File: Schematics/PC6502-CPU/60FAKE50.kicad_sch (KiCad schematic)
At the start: 17 parts, among them J2 Conn_01x02, J3 USB_C_Receptacle_USB2.0_16P, Q1 IRLML6402, U9 FT245RNL

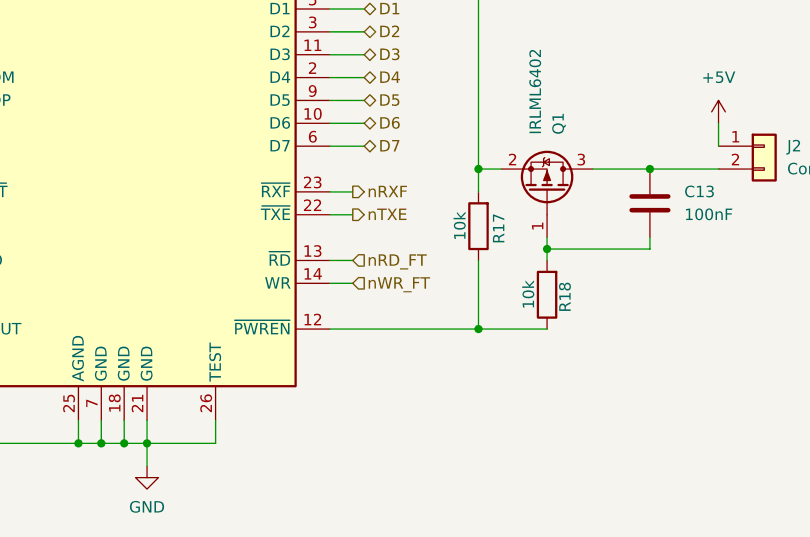
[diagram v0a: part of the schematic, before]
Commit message: FT245 label change
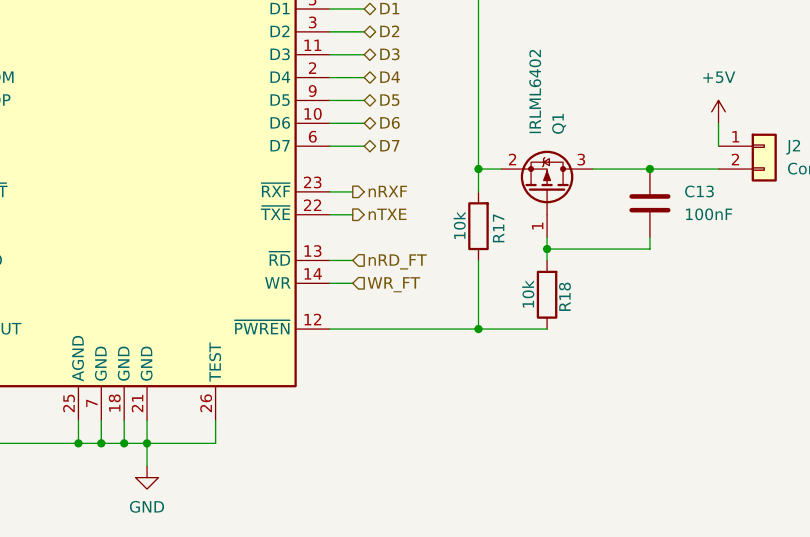
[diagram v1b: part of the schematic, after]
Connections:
- net nWR_FT renamed WR_FT
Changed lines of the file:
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@@
 		)
 	)
-	(hierarchical_label "nWR_FT"
+	(hierarchical_label "WR_FT"
 		(shape input)
 		(at 212.09 114.3 0)

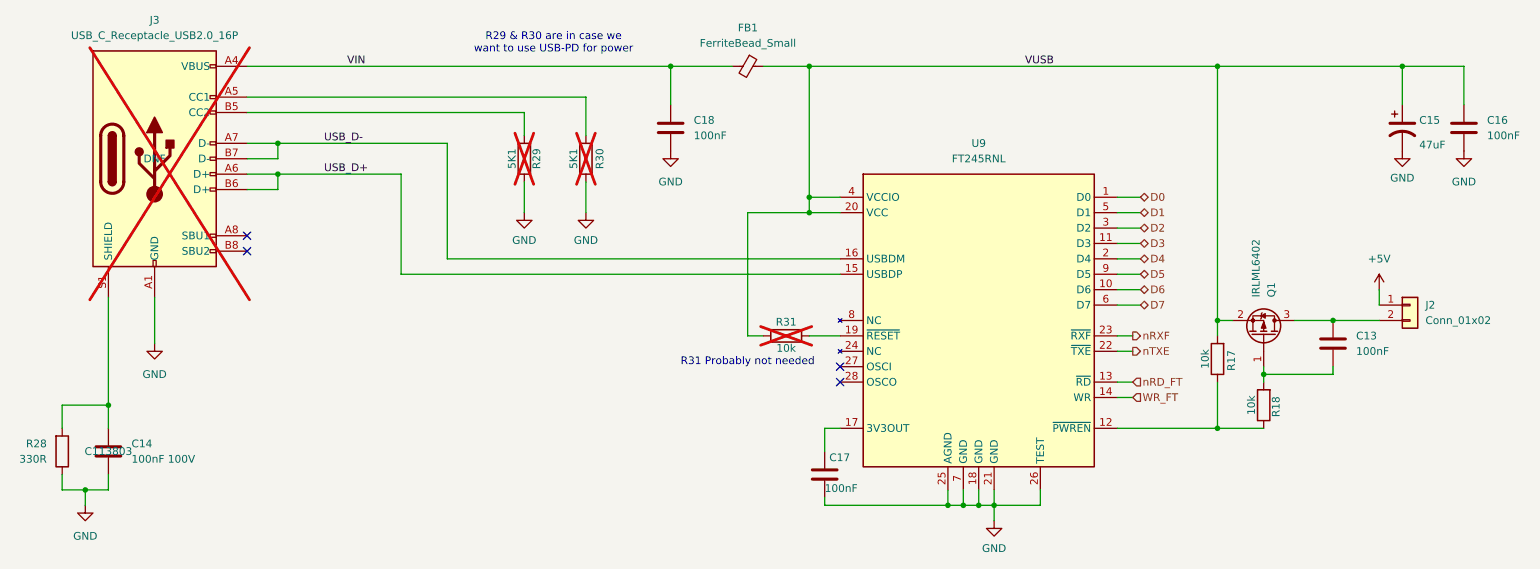
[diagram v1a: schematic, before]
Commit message: V1.1 CPU, VIA and POWER PCBs uploaded
A simpler CPU board (direct link to FT245R, 74161 removed and some tidying of tracks). Fixed a couple of floating inputs to RAM/ROM
VIA is much simpler, having just the one VIA chip.
POWER board has USB-PD and a 24VDC input for higher power stuff in the future.
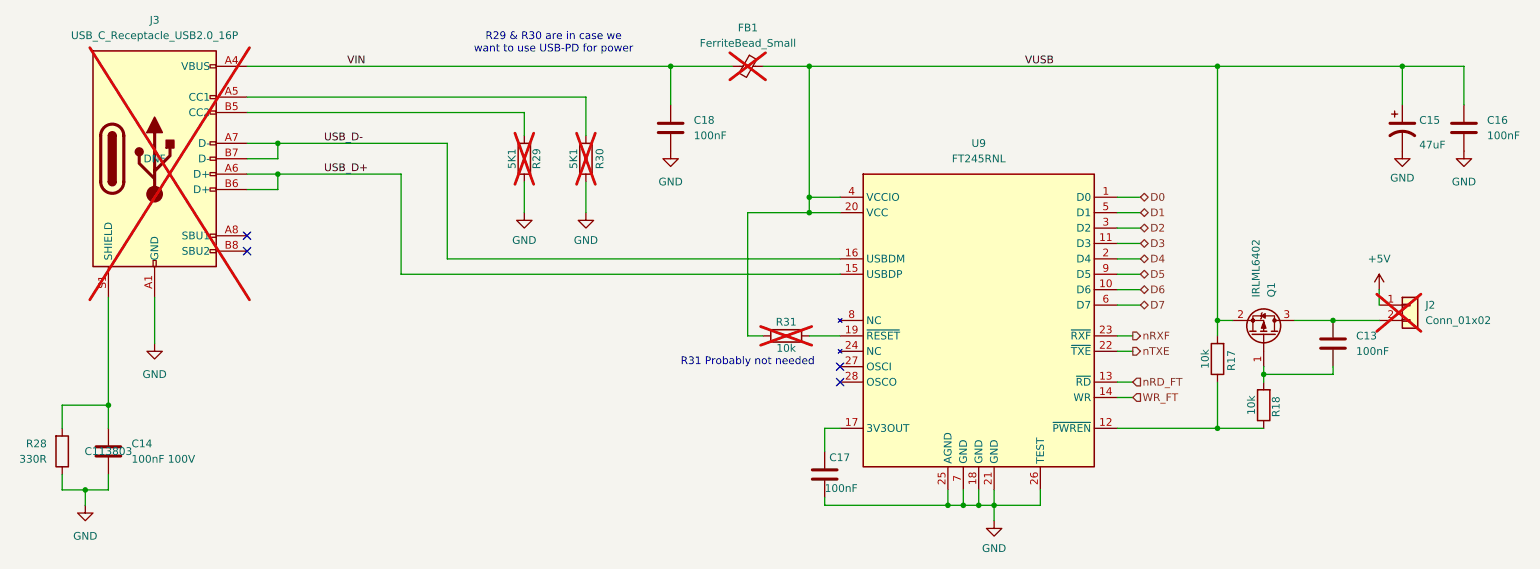
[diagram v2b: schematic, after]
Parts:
- C13, C17: LCSC (none) -> C113803
- C16, C18: LCSC (none) -> C49678
- FB1, J2: LCSC (none) -> DNF; now not fitted
- Q1: LCSC (none) -> C2593
- R17, R18: LCSC (none) -> C25744
- R28: LCSC (none) -> C25104
- R29, R30, R31: LCSC (none) -> DNF
- U9: LCSC (none) -> C6558294
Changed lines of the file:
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@@
 		(in_bom yes)
 		(on_board yes)
-		(dnp no)
+		(dnp yes)
 		(fields_autoplaced yes)
 		(property "Reference" "J2"
@@
 			)
 		)
+		(property "LCSC" "DNF"
+			(at 257.81 99.06 0)
+			(effects
+				(font
+					(size 1.27 1.27)
+				)
+				(hide yes)
+			)
+		)
 		(pin "1"
 		)
@@
 			)
 		)
+		(property "LCSC" "DNF"
+			(at 121.92 74.93 90)
+			(effects
+				(font
+					(size 1.27 1.27)
+				)
+				(hide yes)
+			)
+		)
 		(pin "1"
 		)
@@
 			)
 		)
+		(property "LCSC" "C25744"
+			(at 233.68 115.57 90)
+			(effects
+				(font
+					(size 1.27 1.27)
+				)
+				(hide yes)
+			)
+		)
 		(pin "1"
 		)
@@
 		)
 		(property "Description" ""
+			(at 161.29 127 0)
+			(effects
+				(font
+					(size 1.27 1.27)
+				)
+				(hide yes)
+			)
+		)
+		(property "LCSC" "C113803"
 			(at 161.29 127 0)
 			(effects
@@
 			)
 		)
+		(property "LCSC" "DNF"
+			(at 111.76 74.93 90)
+			(effects
+				(font
+					(size 1.27 1.27)
+				)
+				(hide yes)
+			)
+		)
 		(pin "1"
 		)
@@
 			)
 		)
-		(property "LCSC" ""
+		(property "LCSC" "C25104"
 			(at 35.56 123.19 0)
 			(effects
@@
 			)
 		)
+		(property "LCSC" "C6558294"
+			(at 186.69 101.6 0)
+			(effects
+				(font
+					(size 1.27 1.27)
+				)
+				(hide yes)
+			)
+		)
 		(pin "28"
 		)
@@
 			)
 		)
+		(property "LCSC" "DNF"
+			(at 154.94 104.14 90)
+			(effects
+				(font
+					(size 1.27 1.27)
+				)
+				(hide yes)
+			)
+		)
 		(pin "1"
 		)
@@
 		(property "Description" ""
 			(at 226.06 107.95 0)
+			(effects
+				(font
+					(size 1.27 1.27)
+				)
+				(hide yes)
+			)
+		)
+		(property "LCSC" "C25744"
+			(at 226.06 107.95 90)
 			(effects
 				(font
@@
 			)
 		)
+		(property "LCSC" "C49678"
+			(at 135.89 69.85 0)
+			(effects
+				(font
+					(size 1.27 1.27)
+				)
+				(hide yes)
+			)
+		)
 		(pin "1"
 		)
@@
 		(in_bom yes)
 		(on_board yes)
-		(dnp no)
+		(dnp yes)
 		(fields_autoplaced yes)
 		(property "Reference" "FB1"
@@
 			)
 		)
+		(property "LCSC" "DNF"
+			(at 148.59 59.69 90)
+			(effects
+				(font
+					(size 1.27 1.27)
+				)
+				(hide yes)
+			)
+		)
 		(pin "2"
 		)
@@
 			)
 		)
+		(property "LCSC" "C49678"
+			(at 266.7 69.85 0)
+			(effects
+				(font
+					(size 1.27 1.27)
+				)
+				(hide yes)
+			)
+		)
 		(pin "1"
 		)
@@
 			)
 		)
+		(property "LCSC" "C113803"
+			(at 245.11 105.41 0)
+			(effects
+				(font
+					(size 1.27 1.27)
+				)
+				(hide yes)
+			)
+		)
 		(pin "1"
 		)
@@
 			(at 233.68 104.14 0)
 			(effects
+				(font
+					(size 1.27 1.27)
+				)
+				(hide yes)
+			)
+		)
+		(property "LCSC" "C2593"
+			(at 233.68 104.14 0)
+			(effects

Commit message: Tidy up and simplify
Created schematic for FM & Speech sound board
Made Storage board just for Compact Flash (CF) storage
Routed Storage PCB
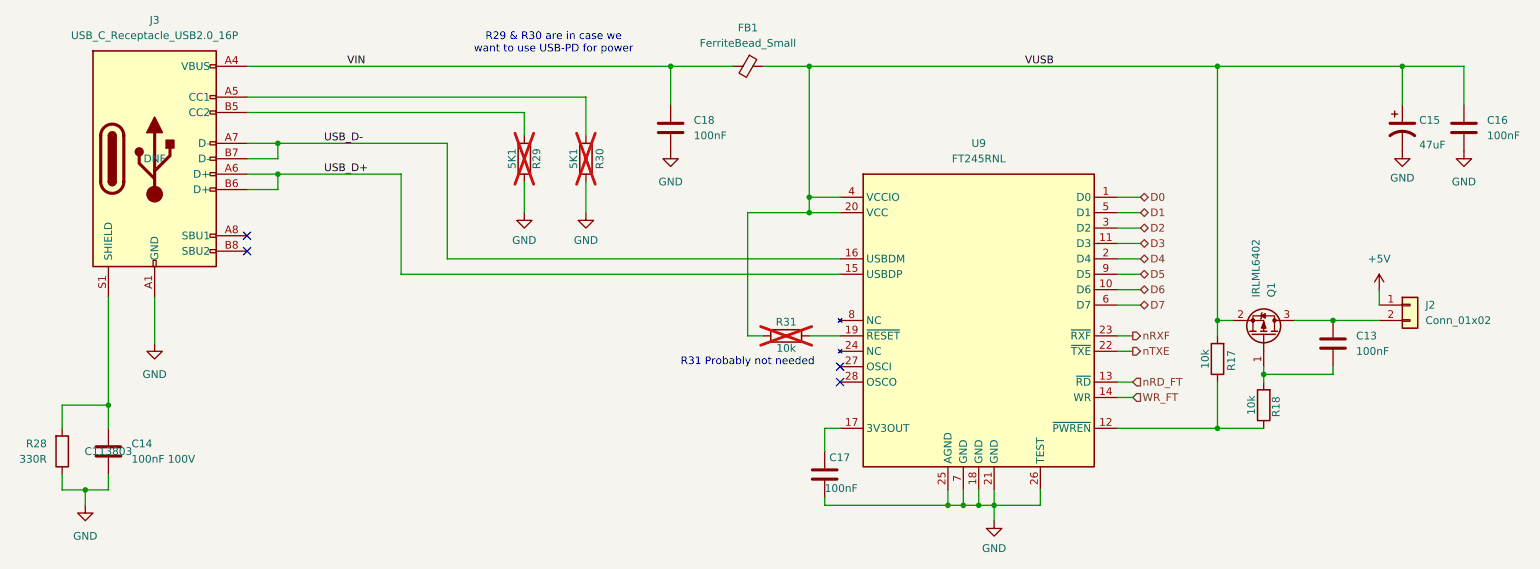
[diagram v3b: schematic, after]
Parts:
- FB1, J2, J3: now fitted
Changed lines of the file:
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@@
 		(in_bom yes)
 		(on_board yes)
-		(dnp yes)
+		(dnp no)
 		(fields_autoplaced yes)
 		(property "Reference" "J3"
@@
 		(in_bom yes)
 		(on_board yes)
-		(dnp yes)
+		(dnp no)
 		(fields_autoplaced yes)
 		(property "Reference" "J2"
@@
 		(in_bom yes)
 		(on_board yes)
-		(dnp yes)
+		(dnp no)
 		(fields_autoplaced yes)
 		(property "Reference" "FB1"
